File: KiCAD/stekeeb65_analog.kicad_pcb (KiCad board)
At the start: 2 copper layers, 211 parts, among them IC1 ADS7953SBDBTR, IC2 ADS7953SBDBTR, IC3 ADS7953SBDBTR, IC4 ADS7953SBDBTR, J1 Conn_01x04, J2 Conn_01x03, SW1 MX_Lekker, SW10 MX_Lekker, SW11 MX_Lekker, SW12 MX_Lekker, SW13 MX_Lekker, SW14 MX_Lekker, SW15 MX_Lekker, SW16 MX_Lekker, SW17 MX_Lekker, SW18 MX_Lekker, SW19 MX_Lekker, SW2 MX_Lekker, SW20 MX_Lekker, SW21 MX_Lekker, SW22 MX_Lekker, SW23 MX_Lekker, SW24 MX_Lekker, SW25 MX_Lekker, SW26 MX_Lekker, SW27 MX_Lekker, SW28 MX_Lekker, SW29 MX_Lekker, SW3 MX_Lekker, SW30 MX_Lekker, SW31 MX_Lekker, SW32 MX_Lekker, SW33 MX_Lekker, SW34 MX_Lekker, SW35 MX_Lekker, SW36 MX_Lekker, SW37 MX_Lekker, SW38 MX_Lekker, SW39 MX_Lekker, SW4 MX_Lekker, SW40 MX_Lekker, SW41 MX_Lekker, SW42 MX_Lekker, SW43 MX_Lekker, SW44 MX_Lekker, SW45 MX_Lekker, SW46 MX_Lekker, SW47 MX_Lekker, SW48 MX_Lekker, SW49 MX_Lekker, SW5 MX_Lekker, SW50 MX_Lekker, SW51 MX_Lekker, SW52 MX_Lekker, SW53 MX_Lekker, SW54 MX_Lekker, SW55 MX_Lekker, SW56 MX_Lekker, SW57 MX_Lekker, SW58 MX_Lekker, SW59 MX_Lekker, SW6 MX_Lekker, SW60 MX_Lekker, SW61 MX_Lekker, SW62 MX_Lekker, SW63 MX_Lekker, SW64 MX_Lekker, SW65 MX_Lekker, SW66 MX_Lekker, SW67 MX_Lekker, SW68 MX_Lekker, SW69 SW_Push, SW7 MX_Lekker, SW71 SW_Push, SW8 MX_Lekker, SW9 MX_Lekker, U1 AH49-E, U10 AH49-E, U11 AH49-E, U12 AH49-E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

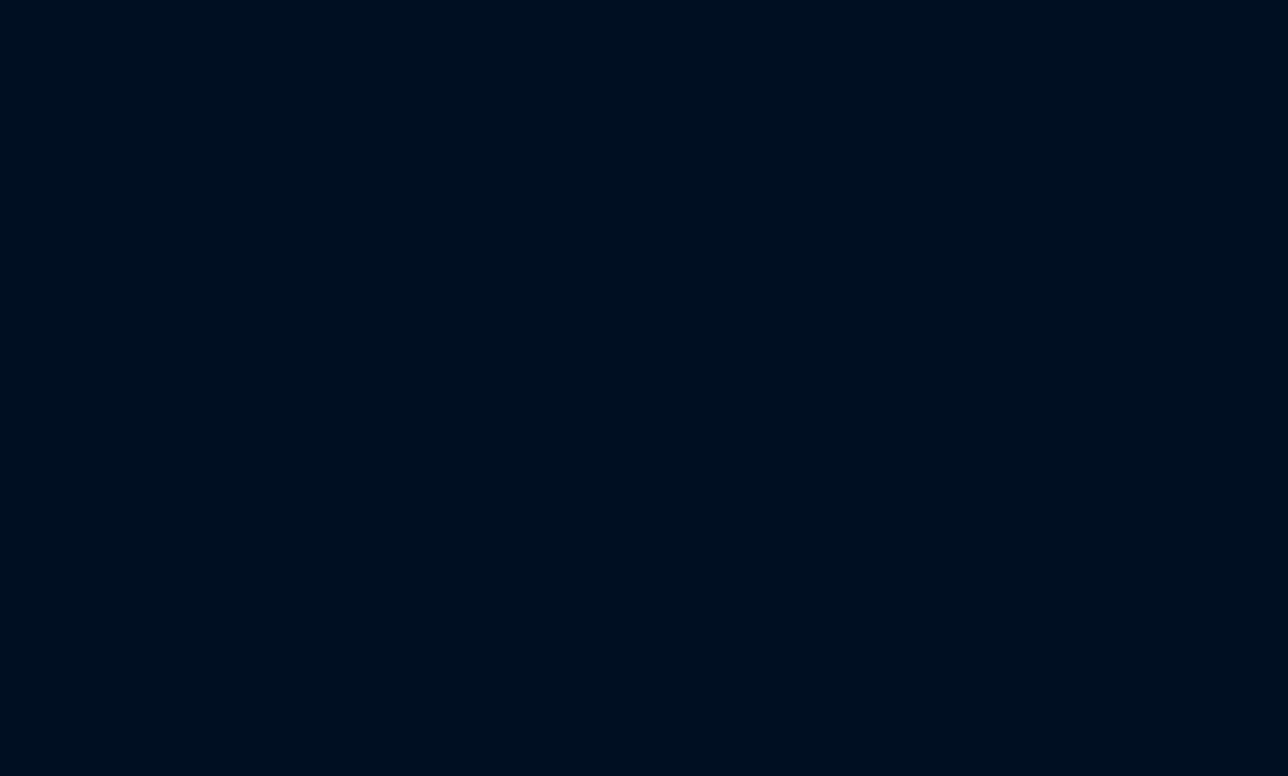
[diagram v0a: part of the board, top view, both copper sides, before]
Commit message: Adding LED library
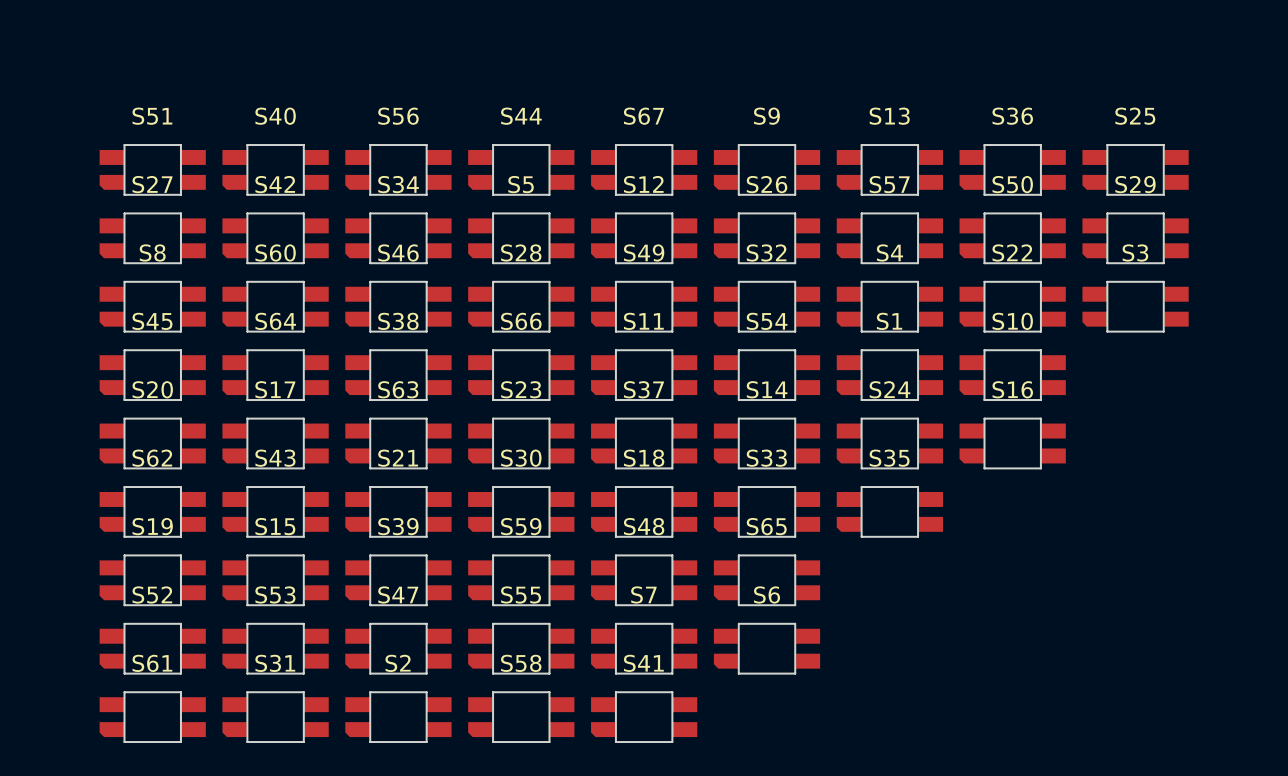
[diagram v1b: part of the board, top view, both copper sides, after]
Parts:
- added S1: QBLP677R-RGB, random-keyboard-parts:QBLP677R-RGB-square_cutout, F.Cu at (108.9, 241.7)
- added S10: QBLP677R-RGB, random-keyboard-parts:QBLP677R-RGB-square_cutout, F.Cu at (116.3, 241.7)
- added S11: QBLP677R-RGB, random-keyboard-parts:QBLP677R-RGB-square_cutout, F.Cu at (94.1, 241.7)
- added S12: QBLP677R-RGB, random-keyboard-parts:QBLP677R-RGB-square_cutout, F.Cu at (94.1, 233.5)
- added S13: QBLP677R-RGB, random-keyboard-parts:QBLP677R-RGB-square_cutout, F.Cu at (108.9, 229.4)
- added S14: QBLP677R-RGB, random-keyboard-parts:QBLP677R-RGB-square_cutout, F.Cu at (101.5, 245.8)
- added S15: QBLP677R-RGB, random-keyboard-parts:QBLP677R-RGB-square_cutout, F.Cu at (71.9, 254.1)
- added S16: QBLP677R-RGB, random-keyboard-parts:QBLP677R-RGB-square_cutout, F.Cu at (116.3, 245.8)
- added S17: QBLP677R-RGB, random-keyboard-parts:QBLP677R-RGB-square_cutout, F.Cu at (71.9, 245.8)
- added S18: QBLP677R-RGB, random-keyboard-parts:QBLP677R-RGB-square_cutout, F.Cu at (94.1, 250.0)
- added S19: QBLP677R-RGB, random-keyboard-parts:QBLP677R-RGB-square_cutout, F.Cu at (64.5, 254.1)
- added S2: QBLP677R-RGB, random-keyboard-parts:QBLP677R-RGB-square_cutout, F.Cu at (79.3, 262.3)
- added S20: QBLP677R-RGB, random-keyboard-parts:QBLP677R-RGB-square_cutout, F.Cu at (64.5, 245.8)
- added S21: QBLP677R-RGB, random-keyboard-parts:QBLP677R-RGB-square_cutout, F.Cu at (79.3, 250.0)
- added S22: QBLP677R-RGB, random-keyboard-parts:QBLP677R-RGB-square_cutout, F.Cu at (116.3, 237.6)
- added S23: QBLP677R-RGB, random-keyboard-parts:QBLP677R-RGB-square_cutout, F.Cu at (86.7, 245.8)
- added S24: QBLP677R-RGB, random-keyboard-parts:QBLP677R-RGB-square_cutout, F.Cu at (108.9, 245.8)
- added S25: QBLP677R-RGB, random-keyboard-parts:QBLP677R-RGB-square_cutout, F.Cu at (123.7, 229.4)
- added S26: QBLP677R-RGB, random-keyboard-parts:QBLP677R-RGB-square_cutout, F.Cu at (101.5, 233.5)
- added S27: QBLP677R-RGB, random-keyboard-parts:QBLP677R-RGB-square_cutout, F.Cu at (64.5, 233.5)
- added S28: QBLP677R-RGB, random-keyboard-parts:QBLP677R-RGB-square_cutout, F.Cu at (86.7, 237.6)
- added S29: QBLP677R-RGB, random-keyboard-parts:QBLP677R-RGB-square_cutout, F.Cu at (123.7, 233.5)
- added S3: QBLP677R-RGB, random-keyboard-parts:QBLP677R-RGB-square_cutout, F.Cu at (123.7, 237.6)
- added S30: QBLP677R-RGB, random-keyboard-parts:QBLP677R-RGB-square_cutout, F.Cu at (86.7, 250.0)
- added S31: QBLP677R-RGB, random-keyboard-parts:QBLP677R-RGB-square_cutout, F.Cu at (71.9, 262.3)
- added S32: QBLP677R-RGB, random-keyboard-parts:QBLP677R-RGB-square_cutout, F.Cu at (101.5, 237.6)
- added S33: QBLP677R-RGB, random-keyboard-parts:QBLP677R-RGB-square_cutout, F.Cu at (101.5, 250.0)
- added S34: QBLP677R-RGB, random-keyboard-parts:QBLP677R-RGB-square_cutout, F.Cu at (79.3, 233.5)
- added S35: QBLP677R-RGB, random-keyboard-parts:QBLP677R-RGB-square_cutout, F.Cu at (108.9, 250.0)
- added S36: QBLP677R-RGB, random-keyboard-parts:QBLP677R-RGB-square_cutout, F.Cu at (116.3, 229.4)
- added S37: QBLP677R-RGB, random-keyboard-parts:QBLP677R-RGB-square_cutout, F.Cu at (94.1, 245.8)
- added S38: QBLP677R-RGB, random-keyboard-parts:QBLP677R-RGB-square_cutout, F.Cu at (79.3, 241.7)
- added S39: QBLP677R-RGB, random-keyboard-parts:QBLP677R-RGB-square_cutout, F.Cu at (79.3, 254.1)
- added S4: QBLP677R-RGB, random-keyboard-parts:QBLP677R-RGB-square_cutout, F.Cu at (108.9, 237.6)
- added S40: QBLP677R-RGB, random-keyboard-parts:QBLP677R-RGB-square_cutout, F.Cu at (71.9, 229.4)
- added S41: QBLP677R-RGB, random-keyboard-parts:QBLP677R-RGB-square_cutout, F.Cu at (94.1, 262.3)
- added S42: QBLP677R-RGB, random-keyboard-parts:QBLP677R-RGB-square_cutout, F.Cu at (71.9, 233.5)
- added S43: QBLP677R-RGB, random-keyboard-parts:QBLP677R-RGB-square_cutout, F.Cu at (71.9, 250.0)
- added S44: QBLP677R-RGB, random-keyboard-parts:QBLP677R-RGB-square_cutout, F.Cu at (86.7, 229.4)
- added S45: QBLP677R-RGB, random-keyboard-parts:QBLP677R-RGB-square_cutout, F.Cu at (64.5, 241.7)
- added S46: QBLP677R-RGB, random-keyboard-parts:QBLP677R-RGB-square_cutout, F.Cu at (79.3, 237.6)
- added S47: QBLP677R-RGB, random-keyboard-parts:QBLP677R-RGB-square_cutout, F.Cu at (79.3, 258.2)
- added S48: QBLP677R-RGB, random-keyboard-parts:QBLP677R-RGB-square_cutout, F.Cu at (94.1, 254.1)
- added S49: QBLP677R-RGB, random-keyboard-parts:QBLP677R-RGB-square_cutout, F.Cu at (94.1, 237.6)
- added S5: QBLP677R-RGB, random-keyboard-parts:QBLP677R-RGB-square_cutout, F.Cu at (86.7, 233.5)
- added S50: QBLP677R-RGB, random-keyboard-parts:QBLP677R-RGB-square_cutout, F.Cu at (116.3, 233.5)
- added S51: QBLP677R-RGB, random-keyboard-parts:QBLP677R-RGB-square_cutout, F.Cu at (64.5, 229.4)
- added S52: QBLP677R-RGB, random-keyboard-parts:QBLP677R-RGB-square_cutout, F.Cu at (64.5, 258.2)
- added S53: QBLP677R-RGB, random-keyboard-parts:QBLP677R-RGB-square_cutout, F.Cu at (71.9, 258.2)
- added S54: QBLP677R-RGB, random-keyboard-parts:QBLP677R-RGB-square_cutout, F.Cu at (101.5, 241.7)
- added S55: QBLP677R-RGB, random-keyboard-parts:QBLP677R-RGB-square_cutout, F.Cu at (86.7, 258.2)
- added S56: QBLP677R-RGB, random-keyboard-parts:QBLP677R-RGB-square_cutout, F.Cu at (79.3, 229.4)
- added S57: QBLP677R-RGB, random-keyboard-parts:QBLP677R-RGB-square_cutout, F.Cu at (108.9, 233.5)
- added S58: QBLP677R-RGB, random-keyboard-parts:QBLP677R-RGB-square_cutout, F.Cu at (86.7, 262.3)
- added S59: QBLP677R-RGB, random-keyboard-parts:QBLP677R-RGB-square_cutout, F.Cu at (86.7, 254.1)
- added S6: QBLP677R-RGB, random-keyboard-parts:QBLP677R-RGB-square_cutout, F.Cu at (101.5, 258.2)
- added S60: QBLP677R-RGB, random-keyboard-parts:QBLP677R-RGB-square_cutout, F.Cu at (71.9, 237.6)
- added S61: QBLP677R-RGB, random-keyboard-parts:QBLP677R-RGB-square_cutout, F.Cu at (64.5, 262.3)
- added S62: QBLP677R-RGB, random-keyboard-parts:QBLP677R-RGB-square_cutout, F.Cu at (64.5, 250.0)
- added S63: QBLP677R-RGB, random-keyboard-parts:QBLP677R-RGB-square_cutout, F.Cu at (79.3, 245.8)
- added S64: QBLP677R-RGB, random-keyboard-parts:QBLP677R-RGB-square_cutout, F.Cu at (71.9, 241.7)
- added S65: QBLP677R-RGB, random-keyboard-parts:QBLP677R-RGB-square_cutout, F.Cu at (101.5, 254.1)
- added S66: QBLP677R-RGB, random-keyboard-parts:QBLP677R-RGB-square_cutout, F.Cu at (86.7, 241.7)
- added S67: QBLP677R-RGB, random-keyboard-parts:QBLP677R-RGB-square_cutout, F.Cu at (94.1, 229.4)
- added S7: QBLP677R-RGB, random-keyboard-parts:QBLP677R-RGB-square_cutout, F.Cu at (94.1, 258.2)
- added S8: QBLP677R-RGB, random-keyboard-parts:QBLP677R-RGB-square_cutout, F.Cu at (64.5, 237.6)
- added S9: QBLP677R-RGB, random-keyboard-parts:QBLP677R-RGB-square_cutout, F.Cu at (101.5, 229.4)
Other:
- board outline added: 3.4 x 3 mm

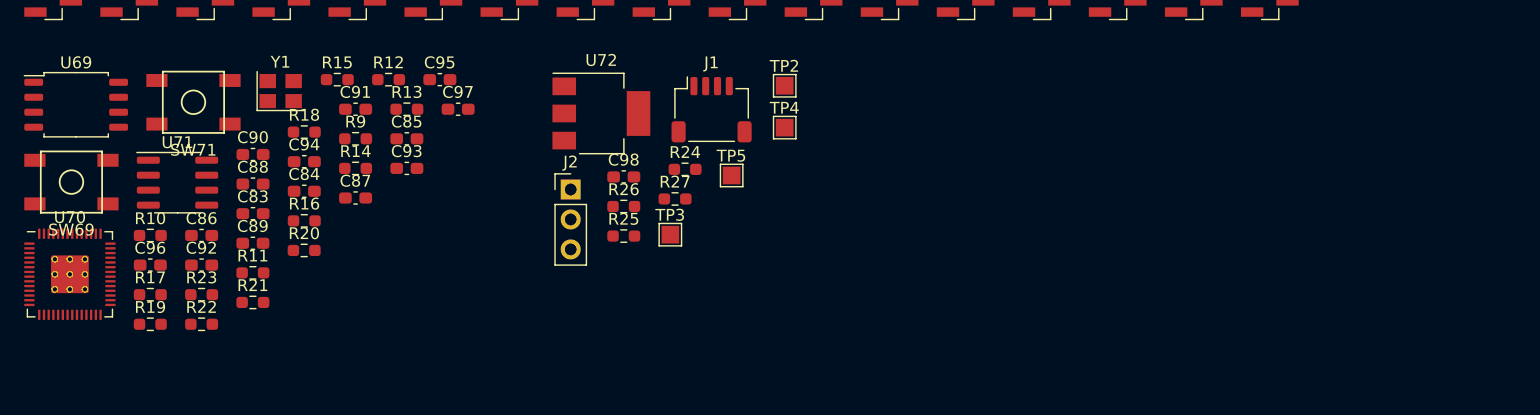
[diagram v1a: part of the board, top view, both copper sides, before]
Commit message: Adding missing led to layout
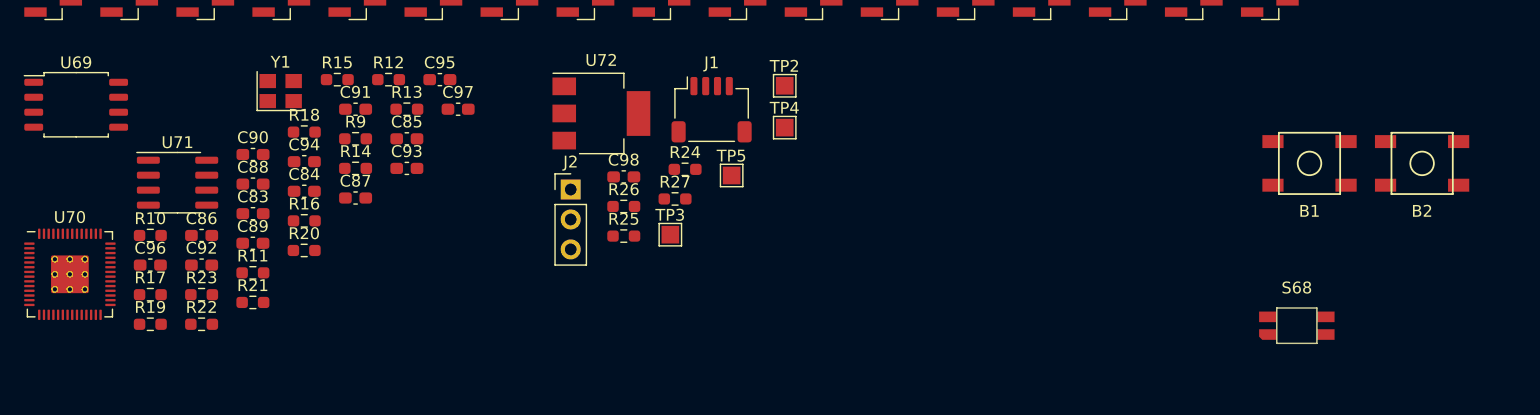
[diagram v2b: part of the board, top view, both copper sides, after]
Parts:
- removed SW69, SW71: SW_Push, random_parts:SKQG-1155865
- added B1: SW_Push, random_parts:SKQG-1155865, F.Cu at (141.8, 196.3)
- added B2: SW_Push, random_parts:SKQG-1155865, F.Cu at (151.3, 196.3)
- added S68: QBLP677R-RGB, random-keyboard-parts:QBLP677R-RGB-square_cutout, F.Cu at (140.7, 210.1)
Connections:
- S15 pad 1: LED_Row_B1 -> LED_Row_B0
- S15 pad 2: LED_Row_G1 -> LED_Row_G0
- S15 pad 3: LED_Row_R1 -> LED_Row_R0
- S15 pad 4: LED1_Col0 -> LED1_Col14
- S16 pad 4: LED1_Col1 -> LED1_Col0
- S17 pad 4: LED1_Col2 -> LED1_Col1
- S18 pad 4: LED1_Col3 -> LED1_Col2
- S19 pad 4: LED1_Col4 -> LED1_Col3
- S20 pad 4: LED1_Col5 -> LED1_Col4
- S21 pad 4: LED1_Col6 -> LED1_Col5
- S22 pad 4: LED1_Col7 -> LED1_Col6
- S23 pad 4: LED1_Col8 -> LED1_Col7
- S24 pad 4: LED1_Col9 -> LED1_Col8
- S25 pad 4: LED1_Col10 -> LED1_Col9
- S26 pad 4: LED1_Col11 -> LED1_Col10
- S27 pad 4: LED1_Col12 -> LED1_Col11
- S28 pad 4: LED1_Col13 -> LED1_Col12
- S29 pad 4: LED1_Col14 -> LED1_Col13
- S30 pad 1: LED_Row_B2 -> LED_Row_B1
- S30 pad 2: LED_Row_G2 -> LED_Row_G1
- S30 pad 3: LED_Row_R2 -> LED_Row_R1
- S30 pad 4: LED2_Col0 -> LED1_Col14
- S31 pad 4: LED2_Col1 -> LED2_Col0
- S32 pad 4: LED2_Col2 -> LED2_Col1
- S33 pad 4: LED2_Col3 -> LED2_Col2
- S34 pad 4: LED2_Col4 -> LED2_Col3
- S35 pad 4: LED2_Col5 -> LED2_Col4
- S36 pad 4: LED2_Col6 -> LED2_Col5
- S37 pad 4: LED2_Col7 -> LED2_Col6
- S38 pad 4: LED2_Col8 -> LED2_Col7
- S39 pad 4: LED2_Col9 -> LED2_Col8
- S40 pad 4: LED2_Col10 -> LED2_Col9
- S41 pad 4: LED2_Col11 -> LED2_Col10
- S42 pad 4: LED2_Col12 -> LED2_Col11
- S43 pad 4: LED2_Col14 -> LED2_Col12
- S44 pad 1: LED_Row_B3 -> LED_Row_B2
- S44 pad 2: LED_Row_G3 -> LED_Row_G2
- S44 pad 3: LED_Row_R3 -> LED_Row_R2
- S44 pad 4: LED2_Col0 -> LED2_Col14
- S45 pad 4: LED2_Col1 -> LED2_Col0
- S46 pad 4: LED2_Col2 -> LED2_Col1
- S47 pad 4: LED2_Col3 -> LED2_Col2
- S48 pad 4: LED2_Col4 -> LED2_Col3
- S49 pad 4: LED2_Col5 -> LED2_Col4
- S50 pad 4: LED2_Col6 -> LED2_Col5
- S51 pad 4: LED2_Col7 -> LED2_Col6
- S52 pad 4: LED2_Col8 -> LED2_Col7
- S53 pad 4: LED2_Col9 -> LED2_Col8
- S54 pad 4: LED2_Col10 -> LED2_Col9
- S55 pad 4: LED2_Col12 -> LED2_Col10
- S56 pad 4: LED2_Col13 -> LED2_Col12
- S57 pad 4: LED2_Col14 -> LED2_Col13
- S58 pad 1: LED_Row_B4 -> LED_Row_B3
- S58 pad 2: LED_Row_G4 -> LED_Row_G3
- S58 pad 3: LED_Row_R4 -> LED_Row_R3
- S58 pad 4: LED2_Col0 -> LED2_Col14
- S59 pad 4: LED2_Col1 -> LED2_Col0
- S60 pad 4: LED2_Col2 -> LED2_Col1
- S61 pad 4: LED2_Col6 -> LED2_Col2
- S62 pad 4: LED2_Col9 -> LED2_Col6
- S63 pad 4: LED2_Col10 -> LED2_Col9
- S64 pad 4: LED2_Col11 -> LED2_Col10
- S65 pad 4: LED2_Col12 -> LED2_Col11
- S66 pad 4: LED2_Col13 -> LED2_Col12
- S67 pad 4: LED2_Col14 -> LED2_Col13

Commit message: updated layout arrangement pre script
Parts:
- B1, B2, C69, C70, C71, C72, C73, C74, C75, C76, C77, C78, C79, C80, C81, C82, C83, C84, C85, C86, C87, C88, C89, C90, C91, C92, C93, C94, C95, C96, C97, C98, IC1, IC2, IC3, IC4, J1, J2, R1, R10, R11, R12, R13, R14, R15, R16, R17, R18, R19, R2, R20, R21, R22, R23, R24, R25, R26, R27, R3, R4, R5, R6, R7, R8, R9, S1, S10, S11, S12, S13, S14, S15, S16, S17, S18, S19, S2, S20, S21, S22, S23, S24, S25, S26, S27, S28, S29, S3, S30, S31, S32, S33, S34, S35, S36, S37, S38, S39, S4, S40, S41, S42, S43, S44, S45, S46, S47, S48, S49, S5, S50, S51, S52, S53, S54, S55, S56, S57, S58, S59, S6, S60, S61, S62, S63, S64, S65, S66, S67, S68, S7, S8, S9, TP1, TP2, TP3, TP4, TP5, U1, U10, U11, U12, U13, U14, U15, U16, U17, U18, U19, U2, U20, U21, U22, U23, U24, U25, U26, U27, U28, U29, U3, U30, U31, U32, U33, U34, U35, U36, U37, U38, U39, U4, U40, U41, U42, U43, U44, U45, U46, U47, U48, U49, U5, U50, U51, U52, U53, U54, U55, U56, U57, U58, U59, U6, U60, U61, U62, U63, U64, U65, U66, U67, U68, U69, U7, U70, U71, U72, U8, U9, Y1: moved to B.Cu
- moved S8 318.4 mm to (364.2, 130.1), turned to 180 degrees
- moved S19 318.4 mm to (364.2, 146.6), turned to 180 degrees
- moved S20 318.4 mm to (364.2, 138.4), turned to 180 degrees
- moved S27 318.4 mm to (364.2, 126.0), turned to 180 degrees
- moved S45 318.4 mm to (364.2, 134.2), turned to 180 degrees
- moved S51 318.4 mm to (364.2, 121.9), turned to 180 degrees
- moved S52 318.4 mm to (364.2, 150.7), turned to 180 degrees
- moved S61 318.4 mm to (364.2, 154.8), turned to 180 degrees
- moved S62 318.4 mm to (364.2, 142.5), turned to 180 degrees
- moved S15 304.5 mm to (356.8, 146.6), turned to 180 degrees
- moved S17 304.5 mm to (356.8, 138.4), turned to 180 degrees
- moved S31 304.5 mm to (356.8, 154.8), turned to 180 degrees
- moved S40 304.5 mm to (356.8, 121.9), turned to 180 degrees
- moved S42 304.5 mm to (356.8, 126.0), turned to 180 degrees
- moved S43 304.5 mm to (356.8, 142.5), turned to 180 degrees
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
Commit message: Kicad being weird
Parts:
- added C1: 0.1u, Capacitor_SMD:C_0603_1608Metric_Pad1.08x0.95mm_HandSolder, B.Cu at (281.6, 211.8)
- added C10: 0.1u, Capacitor_SMD:C_0603_1608Metric_Pad1.08x0.95mm_HandSolder, B.Cu at (286.6, 207.4)
- added C11: 0.1u, Capacitor_SMD:C_0603_1608Metric_Pad1.08x0.95mm_HandSolder, B.Cu at (284.1, 211.8)
- added C12: 0.1u, Capacitor_SMD:C_0603_1608Metric_Pad1.08x0.95mm_HandSolder, B.Cu at (279.1, 203.1)
- added C13: 0.1u, Capacitor_SMD:C_0603_1608Metric_Pad1.08x0.95mm_HandSolder, B.Cu at (284.1, 194.4)
- added C14: 0.1u, Capacitor_SMD:C_0603_1608Metric_Pad1.08x0.95mm_HandSolder, B.Cu at (276.6, 220.5)
- added C15: 0.1u, Capacitor_SMD:C_0603_1608Metric_Pad1.08x0.95mm_HandSolder, B.Cu at (276.6, 203.1)
- added C16: 0.1u, Capacitor_SMD:C_0603_1608Metric_Pad1.08x0.95mm_HandSolder, B.Cu at (274.1, 211.8)
- added C17: 0.1u, Capacitor_SMD:C_0603_1608Metric_Pad1.08x0.95mm_HandSolder, B.Cu at (274.1, 216.1)
- added C18: 0.1u, Capacitor_SMD:C_0603_1608Metric_Pad1.08x0.95mm_HandSolder, B.Cu at (276.6, 207.4)
- added C19: 0.1u, Capacitor_SMD:C_0603_1608Metric_Pad1.08x0.95mm_HandSolder, B.Cu at (271.5, 216.1)
- added C2: 0.1u, Capacitor_SMD:C_0603_1608Metric_Pad1.08x0.95mm_HandSolder, B.Cu at (271.5, 207.4)
- added C20: 0.1u, Capacitor_SMD:C_0603_1608Metric_Pad1.08x0.95mm_HandSolder, B.Cu at (271.5, 211.8)
- added C21: 0.1u, Capacitor_SMD:C_0603_1608Metric_Pad1.08x0.95mm_HandSolder, B.Cu at (269.0, 203.1)
- added C22: 0.1u, Capacitor_SMD:C_0603_1608Metric_Pad1.08x0.95mm_HandSolder, B.Cu at (289.1, 203.1)
- added C23: 0.1u, Capacitor_SMD:C_0603_1608Metric_Pad1.08x0.95mm_HandSolder, B.Cu at (281.6, 203.1)
- added C24: 0.1u, Capacitor_SMD:C_0603_1608Metric_Pad1.08x0.95mm_HandSolder, B.Cu at (286.6, 203.1)
- added C25: 0.1u, Capacitor_SMD:C_0603_1608Metric_Pad1.08x0.95mm_HandSolder, B.Cu at (276.6, 194.4)
- added C26: 0.1u, Capacitor_SMD:C_0603_1608Metric_Pad1.08x0.95mm_HandSolder, B.Cu at (269.0, 220.5)
- added C27: 0.1u, Capacitor_SMD:C_0603_1608Metric_Pad1.08x0.95mm_HandSolder, B.Cu at (269.0, 211.8)
- added C28: 0.1u, Capacitor_SMD:C_0603_1608Metric_Pad1.08x0.95mm_HandSolder, B.Cu at (289.1, 220.5)
- added C29: 0.1u, Capacitor_SMD:C_0603_1608Metric_Pad1.08x0.95mm_HandSolder, B.Cu at (281.6, 190.0)
- added C3: 0.1u, Capacitor_SMD:C_0603_1608Metric_Pad1.08x0.95mm_HandSolder, B.Cu at (274.1, 203.1)
- added C30: 0.1u, Capacitor_SMD:C_0603_1608Metric_Pad1.08x0.95mm_HandSolder, B.Cu at (274.1, 198.7)
- added C31: 0.1u, Capacitor_SMD:C_0603_1608Metric_Pad1.08x0.95mm_HandSolder, B.Cu at (281.6, 207.4)
- added C32: 0.1u, Capacitor_SMD:C_0603_1608Metric_Pad1.08x0.95mm_HandSolder, B.Cu at (269.0, 207.4)
- added C33: 0.1u, Capacitor_SMD:C_0603_1608Metric_Pad1.08x0.95mm_HandSolder, B.Cu at (271.5, 220.5)
- added C34: 0.1u, Capacitor_SMD:C_0603_1608Metric_Pad1.08x0.95mm_HandSolder, B.Cu at (286.6, 198.7)
- added C35: 0.1u, Capacitor_SMD:C_0603_1608Metric_Pad1.08x0.95mm_HandSolder, B.Cu at (284.1, 198.7)
- added C36: 0.1u, Capacitor_SMD:C_0603_1608Metric_Pad1.08x0.95mm_HandSolder, B.Cu at (286.6, 181.3)
- added C37: 0.1u, Capacitor_SMD:C_0603_1608Metric_Pad1.08x0.95mm_HandSolder, B.Cu at (276.6, 198.7)
- added C38: 0.1u, Capacitor_SMD:C_0603_1608Metric_Pad1.08x0.95mm_HandSolder, B.Cu at (279.1, 211.8)
- added C39: 0.1u, Capacitor_SMD:C_0603_1608Metric_Pad1.08x0.95mm_HandSolder, B.Cu at (271.5, 203.1)
- added C4: 0.1u, Capacitor_SMD:C_0603_1608Metric_Pad1.08x0.95mm_HandSolder, B.Cu at (269.0, 216.1)
- added C40: 0.1u, Capacitor_SMD:C_0603_1608Metric_Pad1.08x0.95mm_HandSolder, B.Cu at (279.1, 216.1)
- added C41: 0.1u, Capacitor_SMD:C_0603_1608Metric_Pad1.08x0.95mm_HandSolder, B.Cu at (289.1, 181.3)
- added C42: 0.1u, Capacitor_SMD:C_0603_1608Metric_Pad1.08x0.95mm_HandSolder, B.Cu at (284.1, 220.5)
- added C43: 0.1u, Capacitor_SMD:C_0603_1608Metric_Pad1.08x0.95mm_HandSolder, B.Cu at (289.1, 207.4)
- added C44: 0.1u, Capacitor_SMD:C_0603_1608Metric_Pad1.08x0.95mm_HandSolder, B.Cu at (286.6, 185.7)
- added C45: 0.1u, Capacitor_SMD:C_0603_1608Metric_Pad1.08x0.95mm_HandSolder, B.Cu at (289.1, 198.7)
- added C46: 0.1u, Capacitor_SMD:C_0603_1608Metric_Pad1.08x0.95mm_HandSolder, B.Cu at (289.1, 194.4)
- added C47: 0.1u, Capacitor_SMD:C_0603_1608Metric_Pad1.08x0.95mm_HandSolder, B.Cu at (274.1, 220.5)
- added C48: 0.1u, Capacitor_SMD:C_0603_1608Metric_Pad1.08x0.95mm_HandSolder, B.Cu at (279.1, 220.5)
- added C49: 0.1u, Capacitor_SMD:C_0603_1608Metric_Pad1.08x0.95mm_HandSolder, B.Cu at (279.1, 207.4)
- added C5: 0.1u, Capacitor_SMD:C_0603_1608Metric_Pad1.08x0.95mm_HandSolder, B.Cu at (281.6, 216.1)
- added C50: 0.1u, Capacitor_SMD:C_0603_1608Metric_Pad1.08x0.95mm_HandSolder, B.Cu at (284.1, 185.7)
- added C51: 0.1u, Capacitor_SMD:C_0603_1608Metric_Pad1.08x0.95mm_HandSolder, B.Cu at (281.6, 198.7)
- added C52: 0.1u, Capacitor_SMD:C_0603_1608Metric_Pad1.08x0.95mm_HandSolder, B.Cu at (289.1, 216.1)
- added C53: 0.1u, Capacitor_SMD:C_0603_1608Metric_Pad1.08x0.95mm_HandSolder, B.Cu at (284.1, 207.4)
- added C54: 0.1u, Capacitor_SMD:C_0603_1608Metric_Pad1.08x0.95mm_HandSolder, B.Cu at (279.1, 198.7)
- added C55: 0.1u, Capacitor_SMD:C_0603_1608Metric_Pad1.08x0.95mm_HandSolder, B.Cu at (284.1, 190.0)
- added C56: 0.1u, Capacitor_SMD:C_0603_1608Metric_Pad1.08x0.95mm_HandSolder, B.Cu at (286.6, 216.1)
- added C57: 0.1u, Capacitor_SMD:C_0603_1608Metric_Pad1.08x0.95mm_HandSolder, B.Cu at (284.1, 216.1)
- added C58: 0.1u, Capacitor_SMD:C_0603_1608Metric_Pad1.08x0.95mm_HandSolder, B.Cu at (284.1, 203.1)
- added C59: 0.1u, Capacitor_SMD:C_0603_1608Metric_Pad1.08x0.95mm_HandSolder, B.Cu at (274.1, 207.4)
- added C6: 0.1u, Capacitor_SMD:C_0603_1608Metric_Pad1.08x0.95mm_HandSolder, B.Cu at (289.1, 185.7)
- added C60: 0.1u, Capacitor_SMD:C_0603_1608Metric_Pad1.08x0.95mm_HandSolder, B.Cu at (276.6, 216.1)
- added C61: 0.1u, Capacitor_SMD:C_0603_1608Metric_Pad1.08x0.95mm_HandSolder, B.Cu at (281.6, 220.5)
- added C62: 0.1u, Capacitor_SMD:C_0603_1608Metric_Pad1.08x0.95mm_HandSolder, B.Cu at (286.6, 190.0)
- added C63: 0.1u, Capacitor_SMD:C_0603_1608Metric_Pad1.08x0.95mm_HandSolder, B.Cu at (289.1, 190.0)
- added C64: 0.1u, Capacitor_SMD:C_0603_1608Metric_Pad1.08x0.95mm_HandSolder, B.Cu at (286.6, 194.4)
- added C65: 0.1u, Capacitor_SMD:C_0603_1608Metric_Pad1.08x0.95mm_HandSolder, B.Cu at (286.6, 211.8)
- added C66: 0.1u, Capacitor_SMD:C_0603_1608Metric_Pad1.08x0.95mm_HandSolder, B.Cu at (289.1, 211.8)
- added C67: 0.1u, Capacitor_SMD:C_0603_1608Metric_Pad1.08x0.95mm_HandSolder, B.Cu at (281.6, 194.4)
- added C68: 0.1u, Capacitor_SMD:C_0603_1608Metric_Pad1.08x0.95mm_HandSolder, B.Cu at (276.6, 211.8)
- added C7: 0.1u, Capacitor_SMD:C_0603_1608Metric_Pad1.08x0.95mm_HandSolder, B.Cu at (271.5, 198.7)
- added C8: 0.1u, Capacitor_SMD:C_0603_1608Metric_Pad1.08x0.95mm_HandSolder, B.Cu at (286.6, 220.5)
- added C9: 0.1u, Capacitor_SMD:C_0603_1608Metric_Pad1.08x0.95mm_HandSolder, B.Cu at (279.1, 194.4)
- added IC5: IS31FL3733B-TQLS4, SamacSys_Parts:QFP50P900X900X120-49N, B.Cu at (179.7, 272.5)
- added IC6: IS31FL3733B-TQLS4, SamacSys_Parts:QFP50P900X900X120-49N, B.Cu at (191.2, 272.5)
- moved U48 147.8 mm to (238.1, 249.9), turned to 90 degrees
- moved U8 144.9 mm to (242.7, 249.9), turned to 90 degrees
- moved U12 142.3 mm to (247.2, 249.9), turned to 90 degrees
- moved U54 136.8 mm to (242.7, 243.5), turned to 90 degrees
- moved U30 133.9 mm to (247.2, 243.5), turned to 90 degrees
- moved U27 125.7 mm to (247.2, 237.0), turned to 90 degrees
- moved U31 121.0 mm to (238.8, 228.2), turned to 90 degrees
- moved U41 117.5 mm to (243.3, 228.2), turned to 90 degrees
- moved U19 114.2 mm to (247.9, 228.2), turned to 90 degrees
- moved U57 109.8 mm to (243.3, 221.7), turned to 90 degrees
- moved U65 106.3 mm to (247.9, 221.7), turned to 90 degrees
- moved U4 98.7 mm to (247.9, 215.3), turned to 90 degrees
- moved U20 90.4 mm to (239.1, 199.8), turned to 90 degrees
- moved U2 88.2 mm to (248.0, 206.2), turned to 90 degrees
- moved U5 85.7 mm to (243.7, 199.8), turned to 90 degrees
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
